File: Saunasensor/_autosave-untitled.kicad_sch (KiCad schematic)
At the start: 6 parts, among them J1 Conn_01x02_Pin

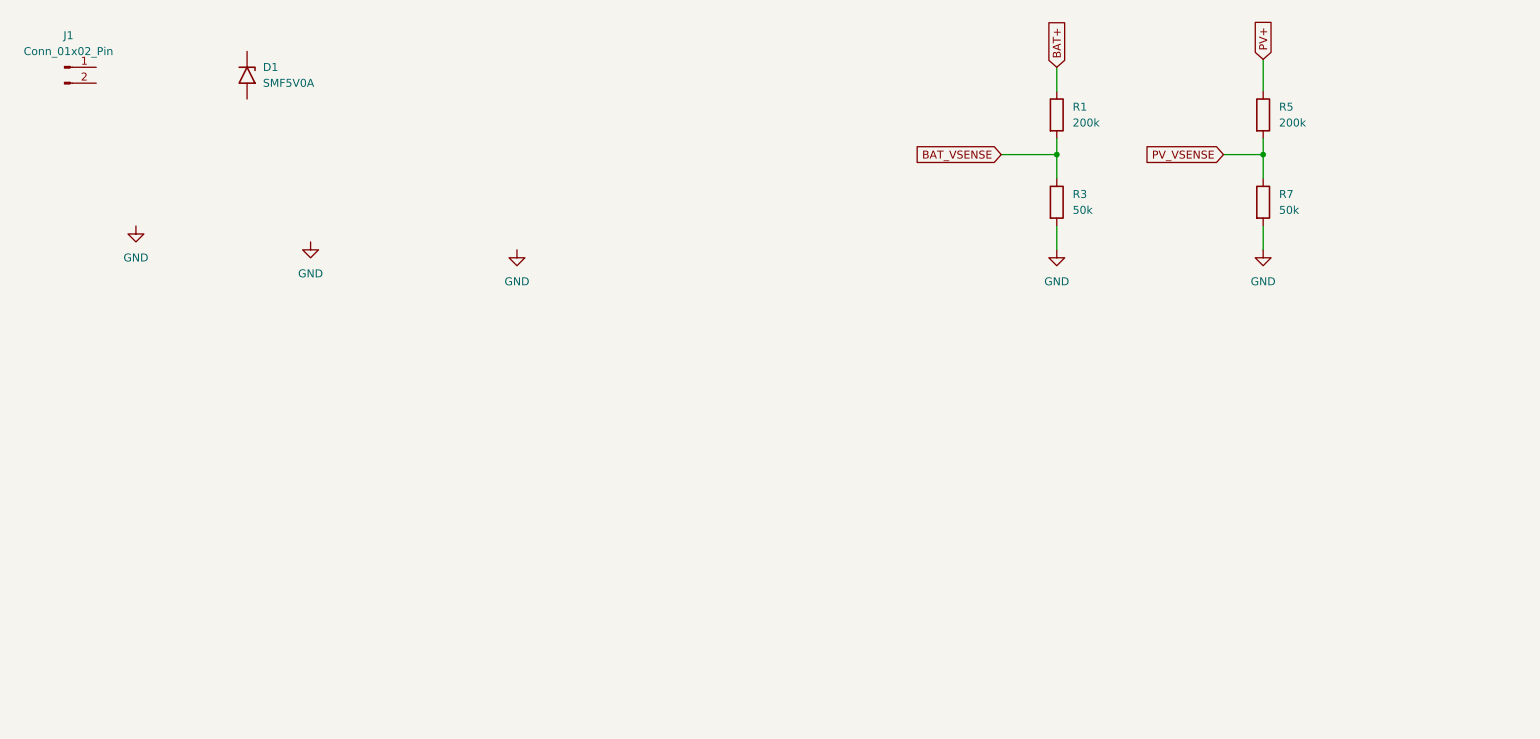
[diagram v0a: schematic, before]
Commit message: Schematic work
* added sensors
* added power supply
* added MCU
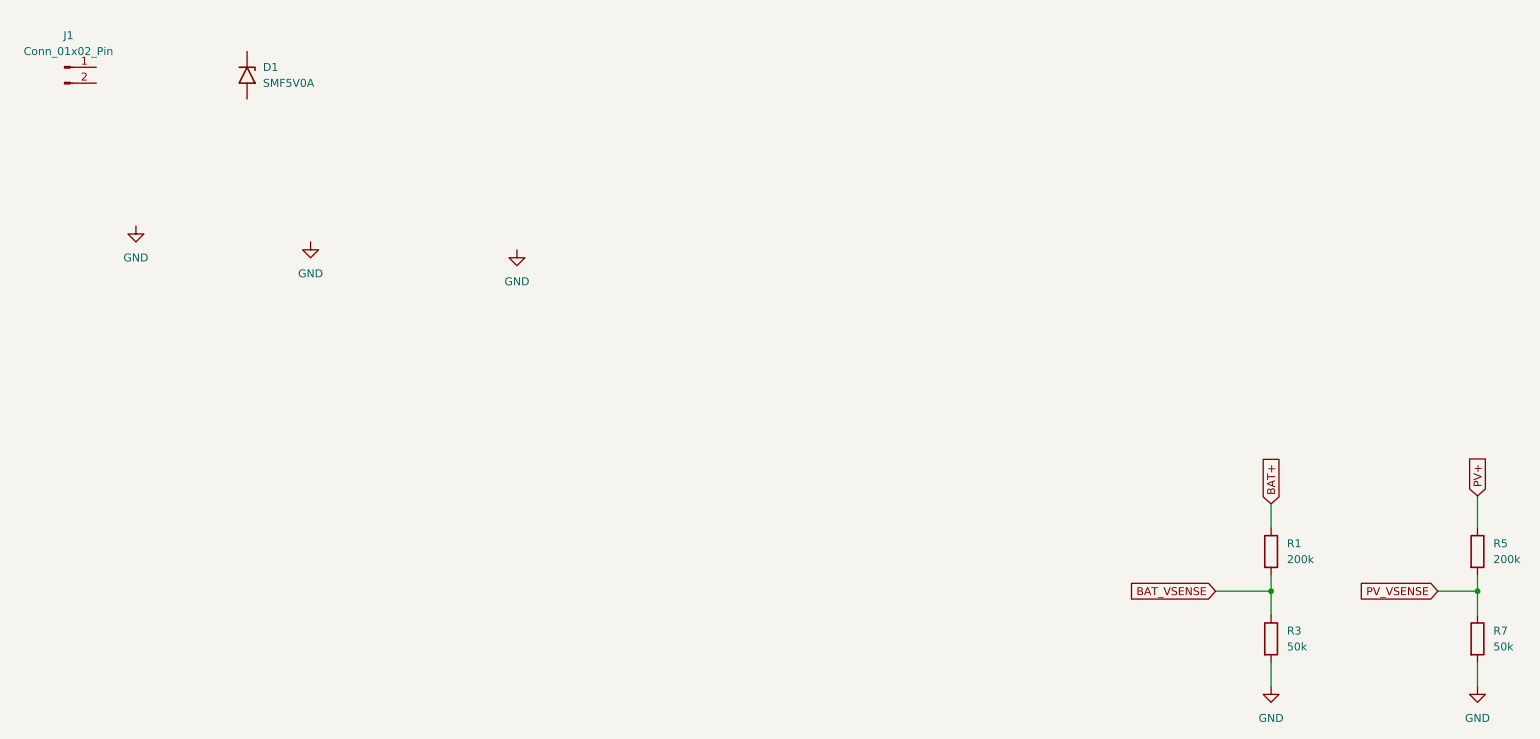
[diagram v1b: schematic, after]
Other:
- moved on the sheet: R1, R3, R5, R7
